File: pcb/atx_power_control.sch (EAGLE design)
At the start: 67 parts, among them IC2 REG1117, IC3 STM32F042F4, IC4 MY_7905DT, J1 ATX24RH, SW1 324_SW, SW2 324_SW, SW3 324_SW, SW4 324_SW, SW5 324_SW, SW7 324_SW, U1 USBC_16P, U2 USBC_16P

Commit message: moved ARGB header, removed GND thermals, jumper pad on USBC data lines, finishing touches
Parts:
- added JP13, JP14: JUMPER-SMT_2_NO_NO-SILK, SparkFun-Jumpers:JUMPER-SMT_2_NO_NO-SILK
- C1, C4: value 1uF -> 100nF; device clock:CAP0805 -> atx_power_control:CAP0805
- C2, C5: value 1uF -> 10uF; device clock:CAP0805 -> atx_power_control:CAP0805
- IC2: device clock:REG1117 -> atx_power_control:REG1117
- JP11: device adafruit_changed:PINHD-1X3CB -> atx_power_control:PINHD-1X3CB
- JP12: device adafruit_changed:PINHD-1X6 -> atx_power_control:PINHD-1X6
- JP2, JP4, JP8: device pinhead:PINHD-1X4 -> atx_power_control:PINHD-1X4
- JP5: device pinhead:PINHD-1X3 -> atx_power_control:PINHD-1X3:1
- JP6: device pinhead:PINHD-1X2 -> atx_power_control:PINHD-1X2
- JP7: device pinhead:PINHD-1X4 -> atx_power_control:PINHD-1X6
- JP9: device pinhead:PINHD-2X4 -> atx_power_control:PINHD-2X4
- R1, R2, R5: value 5.1K -> 5K1; device joyAnalog:RESISTOR0805-RES -> atx_power_control:RESISTOR0805-RES
- R10, R11, R12, R13, R3, R6, R9: value 1K -> 5K1; device SparkFun-Passives:RESISTOR0805-RES -> atx_power_control:RESISTOR0805-RES
- R14, R15: value 5k1 -> 5K1; device SparkFun-Passives:RESISTOR0805-RES -> atx_power_control:RESISTOR0805-RES
- R16, R7: value 5K -> 5K1
- R17, R8: value 5K -> 5K1; device SparkFun-Passives:RESISTOR0805-RES -> atx_power_control:RESISTOR0805-RES
- R4: value 1K -> 5K1
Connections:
- new net N$34: JP13.2, U1.DP1, U1.DP2
- new net N$37: JP12.3, JP14.2, JP7.3
- net N$35: now also JP13.1; no longer U1.DP1, U1.DP2
- net N$36: now also JP14.1; no longer JP12.3, JP7.3
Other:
- moved on the sheet: JP7

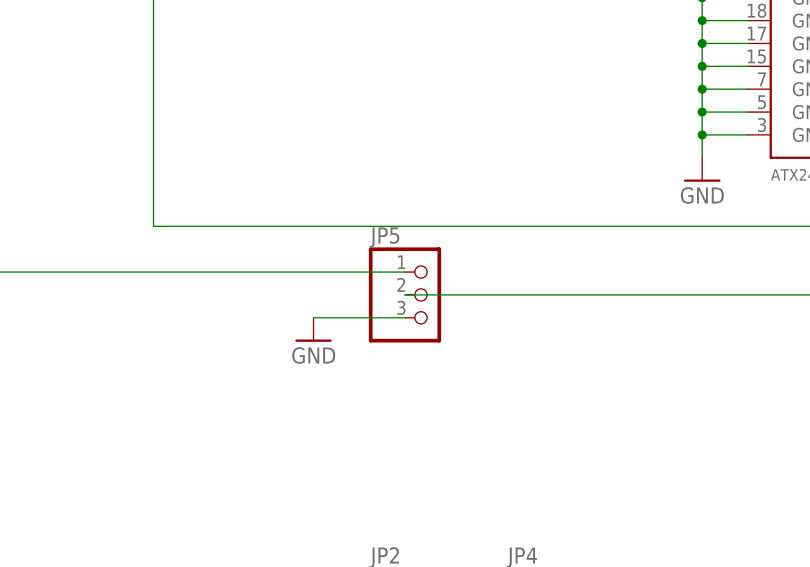
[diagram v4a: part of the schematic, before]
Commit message: wired to softpower by default
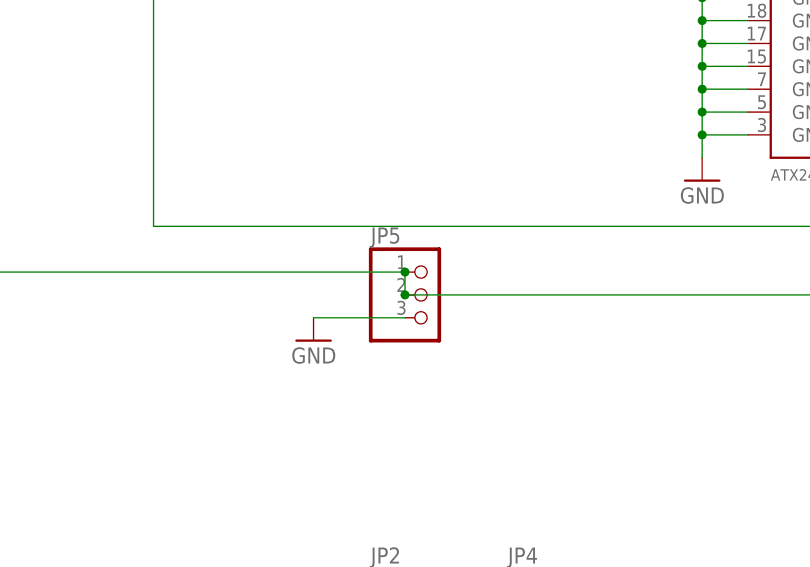
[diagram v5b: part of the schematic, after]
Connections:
- removed net N$24: IC3.PF0/OSC_IN, JP5.1
- net N$25: now also IC3.PF0/OSC_IN, JP5.1
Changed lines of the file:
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@@
 </segment>
 </net>
-<net name="N$24" class="0">
+<net name="N$25" class="0">
 <segment>
+<pinref part="J1" gate="G$1" pin="PS_ON"/>
+<wire x1="259.08" y1="-7.62" x2="248.92" y2="-7.62" width="0.1524" layer="91"/>
+<wire x1="259.08" y1="-33.02" x2="259.08" y2="-7.62" width="0.1524" layer="91"/>
+<pinref part="JP5" gate="A" pin="2"/>
+<wire x1="259.08" y1="-33.02" x2="182.88" y2="-33.02" width="0.1524" layer="91"/>
 <pinref part="IC3" gate="G$1" pin="PF0/OSC_IN"/>
 <wire x1="20.32" y1="27.94" x2="27.94" y2="27.94" width="0.1524" layer="91"/>
@@
 <wire x1="106.68" y1="30.48" x2="106.68" y2="-30.48" width="0.1524" layer="91"/>
 <wire x1="106.68" y1="-30.48" x2="182.88" y2="-30.48" width="0.1524" layer="91"/>
+<wire x1="182.88" y1="-33.02" x2="182.88" y2="-30.48" width="0.1524" layer="91"/>
+<junction x="182.88" y="-33.02"/>
+<junction x="182.88" y="-30.48"/>
 </segment>
 </net>
-<net name="N$25" class="0">
-<segment>
-<pinref part="J1" gate="G$1" pin="PS_ON"/>
-<wire x1="259.08" y1="-7.62" x2="248.92" y2="-7.62" width="0.1524" layer="91"/>
-<wire x1="259.08" y1="-33.02" x2="259.08" y2="-7.62" width="0.1524" layer="91"/>
-<pinref part="JP5" gate="A" pin="2"/>
-<wire x1="259.08" y1="-33.02" x2="182.88" y2="-33.02" width="0.1524" layer="91"/>
-</segment>
-</net>

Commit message: pretty much done
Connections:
- net GND: now also J8.1, JP1.2; no longer R11.1, R12.1
- net N$17: now also J8.2, JP1.1, R11.1, R12.1; no longer J8.1, JP1.2, R11.2, R12.2
- net N$30: now also R11.2, R12.2; no longer J8.2, JP1.1
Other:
- moved on the sheet: J8, JP1, R11, R12
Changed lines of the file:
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@@
 <attribute name="VALUE" x="347.98" y="-10.16" size="1.778" layer="96" rot="R180"/>
 </instance>
-<instance part="R11" gate="G$1" x="317.5" y="71.12" smashed="yes" rot="R270">
-<attribute name="NAME" x="318.9986" y="74.93" size="1.778" layer="95" rot="R270"/>
-<attribute name="VALUE" x="314.198" y="74.93" size="1.778" layer="96" rot="R270"/>
-</instance>
-<instance part="JP1" gate="G$1" x="317.5" y="58.42" smashed="yes" rot="R90">
-<attribute name="NAME" x="311.785" y="52.07" size="1.778" layer="95" rot="R90"/>
-<attribute name="VALUE" x="322.58" y="52.07" size="1.778" layer="96" rot="R90"/>
+<instance part="R11" gate="G$1" x="314.96" y="73.66" smashed="yes" rot="R270">
+<attribute name="NAME" x="316.4586" y="77.47" size="1.778" layer="95" rot="R270"/>
+<attribute name="VALUE" x="311.658" y="77.47" size="1.778" layer="96" rot="R270"/>
+</instance>
+<instance part="JP1" gate="G$1" x="317.5" y="109.22" smashed="yes" rot="R90">
+<attribute name="NAME" x="311.785" y="102.87" size="1.778" layer="95" rot="R90"/>
+<attribute name="VALUE" x="322.58" y="102.87" size="1.778" layer="96" rot="R90"/>
 </instance>
 <instance part="JP2" gate="A" x="185.42" y="-71.12" smashed="yes">
@@
 <attribute name="NAME" x="58.42" y="-13.208" size="1.778" layer="95" font="vector" rot="R180"/>
 </instance>
-<instance part="J8" gate="G$1" x="330.2" y="50.8" smashed="yes" rot="R180">
-<attribute name="VALUE" x="332.74" y="55.626" size="1.778" layer="96" font="vector" rot="R180"/>
-<attribute name="NAME" x="332.74" y="45.212" size="1.778" layer="95" font="vector" rot="R180"/>
+<instance part="J8" gate="G$1" x="330.2" y="101.6" smashed="yes" rot="R180">
+<attribute name="VALUE" x="332.74" y="106.426" size="1.778" layer="96" font="vector" rot="R180"/>
+<attribute name="NAME" x="332.74" y="96.012" size="1.778" layer="95" font="vector" rot="R180"/>
 </instance>
 <instance part="SW5" gate="G$1" x="-132.08" y="43.18" smashed="yes" rot="MR180"/>
@@
 <attribute name="VALUE" x="-190.5" y="53.34" size="1.778" layer="96" rot="MR180"/>
 </instance>
-<instance part="R12" gate="G$1" x="327.66" y="71.12" smashed="yes" rot="R270">
-<attribute name="NAME" x="329.1586" y="74.93" size="1.778" layer="95" rot="R270"/>
-<attribute name="VALUE" x="324.358" y="74.93" size="1.778" layer="96" rot="R270"/>
-</instance>
-<instance part="GND33" gate="1" x="317.5" y="96.52" smashed="yes" rot="R180">
-<attribute name="VALUE" x="320.04" y="99.06" size="1.778" layer="96" rot="R180"/>
+<instance part="R12" gate="G$1" x="322.58" y="73.66" smashed="yes" rot="R270">
+<attribute name="NAME" x="324.0786" y="77.47" size="1.778" layer="95" rot="R270"/>
+<attribute name="VALUE" x="319.278" y="77.47" size="1.778" layer="96" rot="R270"/>
+</instance>
+<instance part="GND33" gate="1" x="317.5" y="147.32" smashed="yes" rot="R180">
+<attribute name="VALUE" x="320.04" y="149.86" size="1.778" layer="96" rot="R180"/>
 </instance>
 <instance part="R13" gate="G$1" x="391.16" y="33.02" smashed="yes" rot="R180">
@@
 </segment>
 <segment>
-<pinref part="GND33" gate="1" pin="GND"/>
-<pinref part="R11" gate="G$1" pin="1"/>
-<wire x1="317.5" y1="93.98" x2="317.5" y2="76.2" width="0.1524" layer="91"/>
-<pinref part="R12" gate="G$1" pin="1"/>
-<wire x1="317.5" y1="76.2" x2="327.66" y2="76.2" width="0.1524" layer="91"/>
-<junction x="317.5" y="76.2"/>
-</segment>
-<segment>
 <pinref part="GND34" gate="1" pin="GND"/>
 <pinref part="JP11" gate="A" pin="3"/>
@@
 <pinref part="LED8" gate="G$1" pin="C"/>
 <pinref part="GND36" gate="1" pin="GND"/>
+</segment>
+<segment>
+<pinref part="J8" gate="G$1" pin="1"/>
+<pinref part="JP1" gate="G$1" pin="2"/>
+<wire x1="317.5" y1="106.68" x2="317.5" y2="101.6" width="0.1524" layer="91"/>
+<wire x1="317.5" y1="101.6" x2="322.58" y2="101.6" width="0.1524" layer="91"/>
+<pinref part="GND33" gate="1" pin="GND"/>
+<wire x1="317.5" y1="144.78" x2="317.5" y2="106.68" width="0.1524" layer="91"/>
+<junction x="317.5" y="106.68"/>
 </segment>
 </net>
@@
 <wire x1="182.88" y1="-66.04" x2="198.12" y2="-66.04" width="0.1524" layer="91"/>
 <junction x="182.88" y="-66.04"/>
-</segment>
-</net>
-<net name="N$17" class="0">
-<segment>
-<pinref part="R11" gate="G$1" pin="2"/>
-<pinref part="JP1" gate="G$1" pin="2"/>
-<wire x1="317.5" y1="66.04" x2="317.5" y2="55.88" width="0.1524" layer="91"/>
-<pinref part="J8" gate="G$1" pin="1"/>
-<wire x1="317.5" y1="55.88" x2="317.5" y2="50.8" width="0.1524" layer="91"/>
-<wire x1="317.5" y1="50.8" x2="322.58" y2="50.8" width="0.1524" layer="91"/>
-<junction x="317.5" y="55.88"/>
-<pinref part="R12" gate="G$1" pin="2"/>
-<wire x1="327.66" y1="66.04" x2="317.5" y2="66.04" width="0.1524" layer="91"/>
-<junction x="317.5" y="66.04"/>
 </segment>
 </net>
@@
 <net name="N$30" class="0">
 <segment>
-<pinref part="JP1" gate="G$1" pin="1"/>
-<wire x1="314.96" y1="55.88" x2="314.96" y2="48.26" width="0.1524" layer="91"/>
-<pinref part="J8" gate="G$1" pin="2"/>
-<wire x1="322.58" y1="48.26" x2="314.96" y2="48.26" width="0.1524" layer="91"/>
 <pinref part="LED7" gate="G$1" pin="A"/>
 <wire x1="307.34" y1="40.64" x2="314.96" y2="40.64" width="0.1524" layer="91"/>
@@
 <wire x1="307.34" y1="132.08" x2="294.64" y2="132.08" width="0.1524" layer="91"/>
 <junction x="307.34" y="68.58"/>
-<wire x1="314.96" y1="48.26" x2="314.96" y2="40.64" width="0.1524" layer="91"/>
-<junction x="314.96" y="48.26"/>
 <junction x="314.96" y="40.64"/>
 <pinref part="U$8" gate="G$1" pin="B0"/>
@@
 <wire x1="276.86" y1="68.58" x2="299.72" y2="71.12" width="0.1524" layer="91"/>
 <junction x="299.72" y="71.12"/>
+<wire x1="314.96" y1="68.58" x2="314.96" y2="40.64" width="0.1524" layer="91"/>
+<pinref part="R11" gate="G$1" pin="2"/>
+<pinref part="R12" gate="G$1" pin="2"/>
+<wire x1="322.58" y1="68.58" x2="314.96" y2="68.58" width="0.1524" layer="91"/>
+<junction x="314.96" y="68.58"/>
 </segment>
 </net>
@@
 </segment>
 </net>
+<net name="N$17" class="0">
+<segment>
+<pinref part="JP1" gate="G$1" pin="1"/>
+<wire x1="314.96" y1="106.68" x2="314.96" y2="99.06" width="0.1524" layer="91"/>
+<pinref part="J8" gate="G$1" pin="2"/>
+<wire x1="322.58" y1="99.06" x2="314.96" y2="99.06" width="0.1524" layer="91"/>
+<junction x="314.96" y="99.06"/>
+<wire x1="314.96" y1="99.06" x2="314.96" y2="78.74" width="0.1524" layer="91"/>
+<pinref part="R11" gate="G$1" pin="1"/>
+<pinref part="R12" gate="G$1" pin="1"/>
+<wire x1="314.96" y1="78.74" x2="322.58" y2="78.74" width="0.1524" layer="91"/>
+<junction x="314.96" y="78.74"/>
+</segment>
+</net>
